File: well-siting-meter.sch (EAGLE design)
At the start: 47 parts, among them J2 7805, T1 MOSFET-NCHANNELFQP30N06L, U1 LCD-16X2NOHOLES, U2 ARDUINO_PRO_MINI, U3 EC2, U4 EC2, U5 AD623, U6 AD623, U7 MAX1771

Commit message: rev A updates, arduino testing
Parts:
- C1, C4: device SparkFun-Passives:CAP_POLPTH1 -> SparkFun-Passives:CAP_POLPTH4
- Q1, Q2: device SparkFun-DiscreteSemi:TRANSISTOR_NPNP2N2222A -> SparkFun-DiscreteSemi:TRANSISTOR_NPNTO92
- R3, R4: value 10K -> 390
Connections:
- net N$1: now also U4.1; no longer U4.12
- net N$4: now also U3.1; no longer U3.12
- net V_BATT: now also U3.12, U4.12; no longer U3.1, U4.1
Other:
- moved on the sheet: Q1, Q2, R3, R4

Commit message: rev A, bom updates
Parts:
- R3, R4: value 390 -> 392R; PN 10.0KXBK-ND -> 392XBK-ND
- RSENSE: value 0R050 -> 0R010; PN 696-1731-ND -> 696-1729-ND
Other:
- moved on the sheet: U1
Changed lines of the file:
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@@
 <attribute name="PN" value="10.0KXBK-ND"/>
 </part>
-<part name="R3" library="SparkFun-Passives" deviceset="RESISTOR" device="PTH-1/4W" value="390">
-<attribute name="PN" value="10.0KXBK-ND"/>
-</part>
-<part name="R4" library="SparkFun-Passives" deviceset="RESISTOR" device="PTH-1/4W" value="390">
-<attribute name="PN" value="10.0KXBK-ND"/>
+<part name="R3" library="SparkFun-Passives" deviceset="RESISTOR" device="PTH-1/4W" value="392R">
+<attribute name="PN" value="392XBK-ND"/>
+</part>
+<part name="R4" library="SparkFun-Passives" deviceset="RESISTOR" device="PTH-1/4W" value="392R">
+<attribute name="PN" value="392XBK-ND"/>
 </part>
 <part name="SUPPLY2" library="SparkFun-Aesthetics" deviceset="5V" device=""/>
@@
 <attribute name="PN" value="EGP20FCT-ND"/>
 </part>
-<part name="RSENSE" library="SparkFun-Passives" deviceset="RESISTOR" device="PTH-1W" value="0R050">
-<attribute name="PN" value="696-1731-ND"/>
+<part name="RSENSE" library="SparkFun-Passives" deviceset="RESISTOR" device="PTH-1W" value="0R010">
+<attribute name="PN" value="696-1729-ND"/>
 </part>
 <part name="R8" library="SparkFun-Passives" deviceset="RESISTOR" device="PTH-1/4W" value="10K">
@@
 <instance part="SUPPLY8" gate="G$1" x="25.4" y="86.36"/>
 <instance part="GND8" gate="1" x="25.4" y="48.26"/>
-<instance part="U1" gate="G$1" x="154.94" y="66.04">
-<attribute name="PN" x="154.94" y="66.04" size="1.778" layer="96" display="off"/>
-</instance>
-<instance part="GND11" gate="1" x="142.24" y="43.18"/>
-<instance part="SUPPLY11" gate="G$1" x="139.7" y="88.9"/>
+<instance part="U1" gate="G$1" x="147.32" y="66.04">
+<attribute name="PN" x="147.32" y="66.04" size="1.778" layer="96" display="off"/>
+</instance>
+<instance part="GND11" gate="1" x="134.62" y="43.18"/>
+<instance part="SUPPLY11" gate="G$1" x="132.08" y="88.9"/>
 <instance part="J12" gate="G$1" x="167.64" y="50.8" rot="MR0">
 <attribute name="PN" x="167.64" y="50.8" size="1.778" layer="96" rot="MR0" display="off"/>
@@
 <segment>
 <pinref part="GND11" gate="1" pin="GND"/>
-<wire x1="142.24" y1="45.72" x2="142.24" y2="48.26" width="0.1524" layer="91"/>
+<wire x1="134.62" y1="45.72" x2="134.62" y2="48.26" width="0.1524" layer="91"/>
 <pinref part="U1" gate="G$1" pin="R/W"/>
-<wire x1="142.24" y1="48.26" x2="142.24" y2="76.2" width="0.1524" layer="91"/>
-<wire x1="142.24" y1="76.2" x2="144.78" y2="76.2" width="0.1524" layer="91"/>
-<junction x="142.24" y="76.2"/>
-<wire x1="142.24" y1="76.2" x2="142.24" y2="86.36" width="0.1524" layer="91"/>
+<wire x1="134.62" y1="48.26" x2="134.62" y2="76.2" width="0.1524" layer="91"/>
+<wire x1="134.62" y1="76.2" x2="137.16" y2="76.2" width="0.1524" layer="91"/>
+<junction x="134.62" y="76.2"/>
+<wire x1="134.62" y1="76.2" x2="134.62" y2="86.36" width="0.1524" layer="91"/>
 <pinref part="U1" gate="G$1" pin="VSS"/>
-<wire x1="142.24" y1="86.36" x2="144.78" y2="86.36" width="0.1524" layer="91"/>
-<junction x="142.24" y="48.26"/>
+<wire x1="134.62" y1="86.36" x2="137.16" y2="86.36" width="0.1524" layer="91"/>
+<junction x="134.62" y="48.26"/>
 <pinref part="U1" gate="G$1" pin="K"/>
-<wire x1="144.78" y1="48.26" x2="142.24" y2="48.26" width="0.1524" layer="91"/>
+<wire x1="137.16" y1="48.26" x2="134.62" y2="48.26" width="0.1524" layer="91"/>
 </segment>
 <segment>
@@
 <segment>
 <pinref part="SUPPLY11" gate="G$1" pin="5V"/>
-<wire x1="139.7" y1="88.9" x2="139.7" y2="83.82" width="0.1524" layer="91"/>
+<wire x1="132.08" y1="88.9" x2="132.08" y2="83.82" width="0.1524" layer="91"/>
 <pinref part="U1" gate="G$1" pin="VDD"/>
-<wire x1="139.7" y1="83.82" x2="144.78" y2="83.82" width="0.1524" layer="91"/>
-<wire x1="139.7" y1="83.82" x2="139.7" y2="50.8" width="0.1524" layer="91"/>
+<wire x1="132.08" y1="83.82" x2="137.16" y2="83.82" width="0.1524" layer="91"/>
+<wire x1="132.08" y1="83.82" x2="132.08" y2="50.8" width="0.1524" layer="91"/>
 <pinref part="U1" gate="G$1" pin="A"/>
-<wire x1="139.7" y1="50.8" x2="144.78" y2="50.8" width="0.1524" layer="91"/>
-<junction x="139.7" y="83.82"/>
+<wire x1="132.08" y1="50.8" x2="137.16" y2="50.8" width="0.1524" layer="91"/>
+<junction x="132.08" y="83.82"/>
 </segment>
 </net>
@@
 <segment>
 <pinref part="U1" gate="G$1" pin="RS"/>
-<wire x1="144.78" y1="78.74" x2="134.62" y2="78.74" width="0.1524" layer="91"/>
-<label x="134.62" y="78.74" size="1.778" layer="95"/>
+<wire x1="137.16" y1="78.74" x2="127" y2="78.74" width="0.1524" layer="91"/>
+<label x="127" y="78.74" size="1.778" layer="95"/>
 </segment>
 <segment>
@@
 <segment>
 <pinref part="U1" gate="G$1" pin="E"/>
-<wire x1="144.78" y1="73.66" x2="134.62" y2="73.66" width="0.1524" layer="91"/>
-<label x="134.62" y="73.66" size="1.778" layer="95"/>
+<wire x1="137.16" y1="73.66" x2="127" y2="73.66" width="0.1524" layer="91"/>
+<label x="127" y="73.66" size="1.778" layer="95"/>
 </segment>
 <segment>
@@
 <segment>
 <pinref part="U1" gate="G$1" pin="DB7"/>
-<wire x1="144.78" y1="53.34" x2="134.62" y2="53.34" width="0.1524" layer="91"/>
-<label x="134.62" y="53.34" size="1.778" layer="95"/>
+<wire x1="137.16" y1="53.34" x2="127" y2="53.34" width="0.1524" layer="91"/>
+<label x="127" y="53.34" size="1.778" layer="95"/>
 </segment>
 <segment>
@@
 <segment>
 <pinref part="U1" gate="G$1" pin="DB6"/>
-<wire x1="144.78" y1="55.88" x2="134.62" y2="55.88" width="0.1524" layer="91"/>
-<label x="134.62" y="55.88" size="1.778" layer="95"/>
+<wire x1="137.16" y1="55.88" x2="127" y2="55.88" width="0.1524" layer="91"/>
+<label x="127" y="55.88" size="1.778" layer="95"/>
 </segment>
 <segment>
@@
 <segment>
 <pinref part="U1" gate="G$1" pin="DB5"/>
-<wire x1="144.78" y1="58.42" x2="134.62" y2="58.42" width="0.1524" layer="91"/>
-<label x="134.62" y="58.42" size="1.778" layer="95"/>
+<wire x1="137.16" y1="58.42" x2="127" y2="58.42" width="0.1524" layer="91"/>
+<label x="127" y="58.42" size="1.778" layer="95"/>
 </segment>
 <segment>
@@
 <segment>
 <pinref part="U1" gate="G$1" pin="DB4"/>
-<wire x1="144.78" y1="60.96" x2="134.62" y2="60.96" width="0.1524" layer="91"/>
-<label x="134.62" y="60.96" size="1.778" layer="95"/>
+<wire x1="137.16" y1="60.96" x2="127" y2="60.96" width="0.1524" layer="91"/>
+<label x="127" y="60.96" size="1.778" layer="95"/>
 </segment>
 <segment>
@@
 <segment>
 <pinref part="U1" gate="G$1" pin="VO"/>
-<wire x1="144.78" y1="81.28" x2="134.62" y2="81.28" width="0.1524" layer="91"/>
-<label x="134.62" y="81.28" size="1.778" layer="95"/>
-</segment>
-<segment>
+<wire x1="137.16" y1="81.28" x2="127" y2="81.28" width="0.1524" layer="91"/>
+<label x="127" y="81.28" size="1.778" layer="95"/>
+</segment>
+<segment>

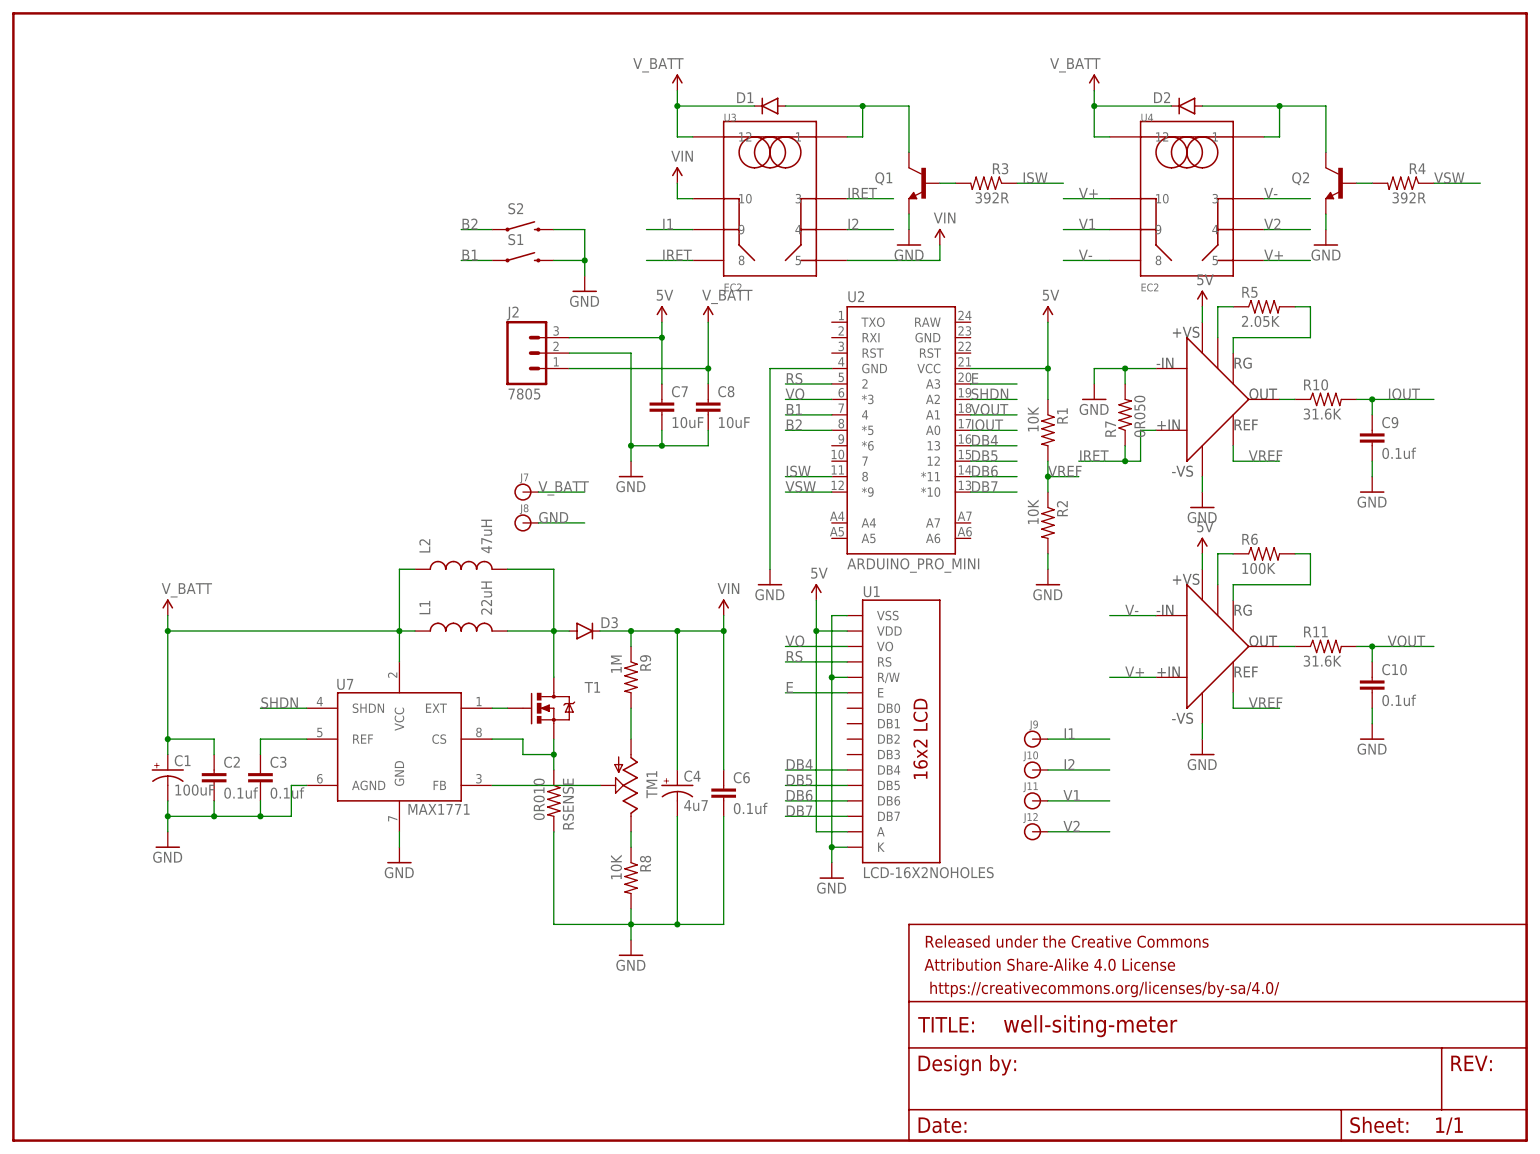
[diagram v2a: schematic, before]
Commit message: start of rev B updates (added relay, AD629, fuse)
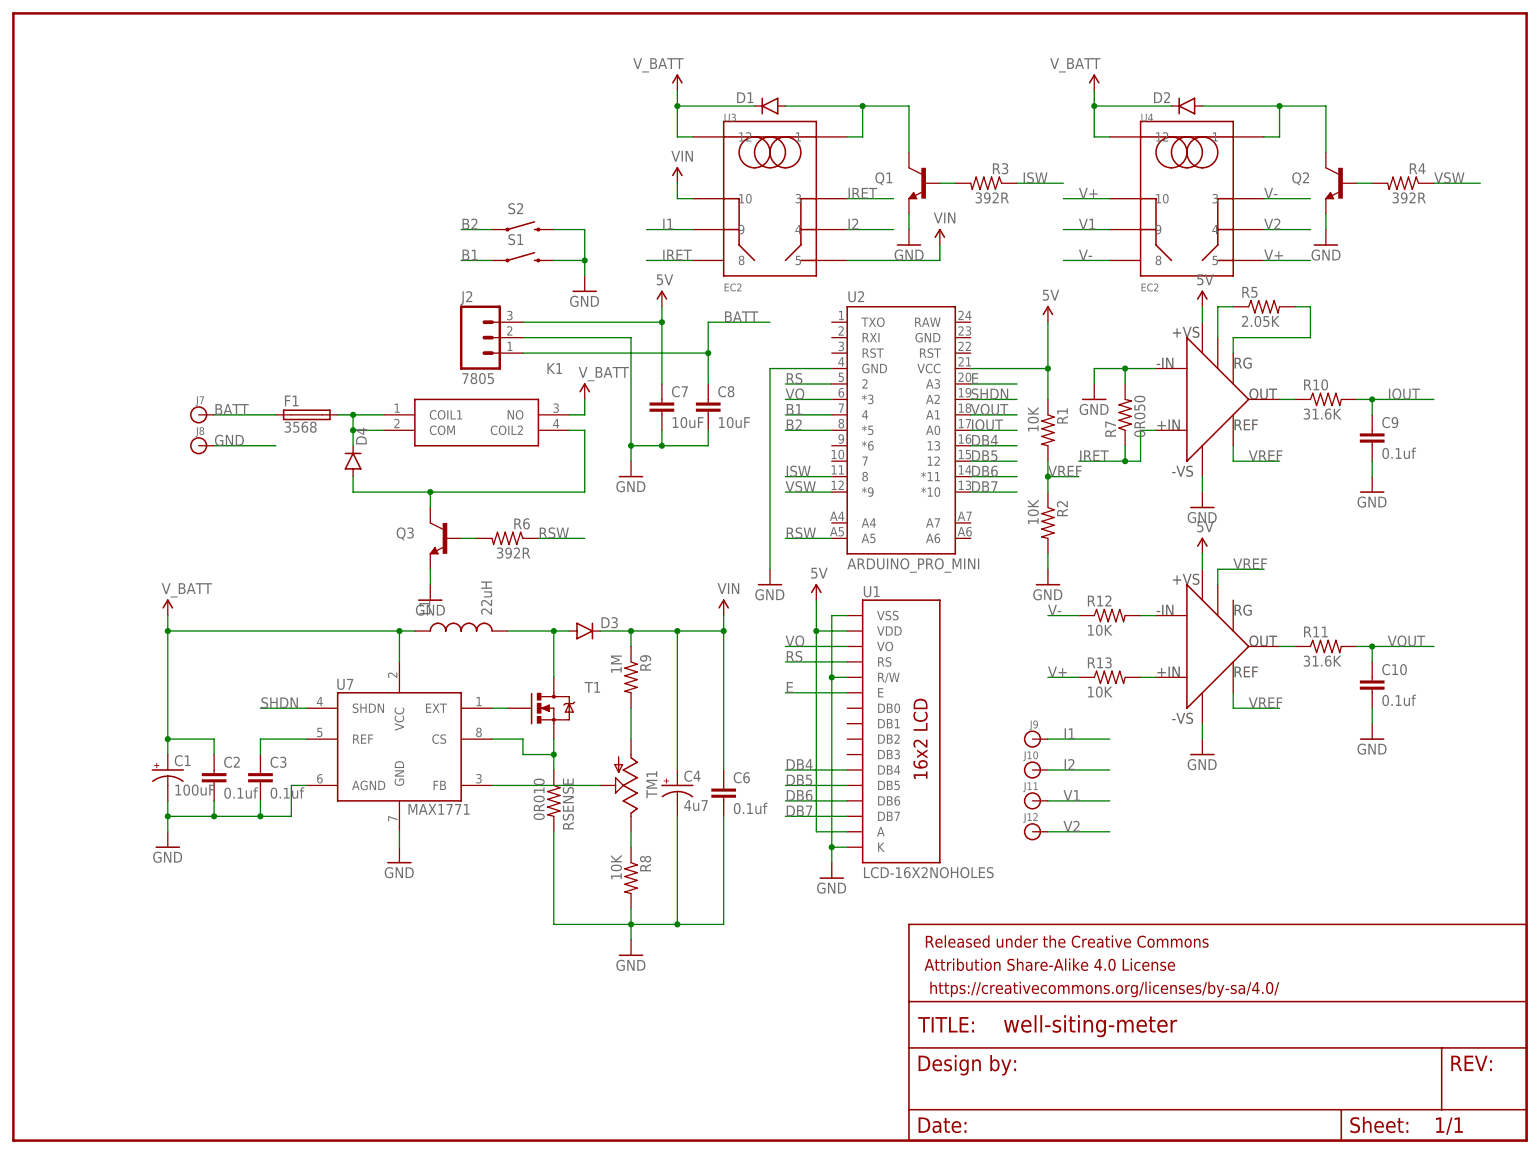
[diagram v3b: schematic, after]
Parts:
- removed L2: 47uH, murata1400:MURATA1400
- added D4: (no value), SparkFun-DiscreteSemi:DIODEPTH
- added F1: 3568, keystone:3568
- added K1: OJE-SH-105HM,000, oje:OJE-SH-105HM,000
- added Q3: (no value), SparkFun-DiscreteSemi:TRANSISTOR_NPNTO92
- added R12, R13: 10K, SparkFun-Passives:RESISTORPTH-1/4W
- R6: value 100K -> 392R; PN 100KXBK-ND -> 392XBK-ND
- U6: value AD623 -> AD629; PN AD623ANZ-ND -> AD629ANZ-ND
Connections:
- removed net N$26: R6.1, U6.-RG
- removed net N$27: R6.2, U6.+RG
- new net BATT: C8.1, F1.1, J2.1, J7.1
- new net FUSE: D4.C, F1.2, K1.COIL1, K1.COM
- new net N$13: R12.2, U6.-IN
- new net N$16: R13.2, U6.+IN
- new net N$17: D4.A, K1.COIL2, Q3.C
- new net N$18: Q3.B, R6.2
- new net RSW: R6.1, U2.A5
- net GND: now also Q3.E
- net N$9: no longer L2.2
- net V+: now also R13.1; no longer U6.+IN
- net V-: now also R12.1; no longer U6.-IN
- net VREF: now also U6.-RG
- net V_BATT: now also K1.NO; no longer C8.1, J2.1, J7.1, L2.1
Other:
- moved on the sheet: J2, J7, J8, R6
